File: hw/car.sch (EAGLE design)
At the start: 21 parts, among them Q1 BS170, Q2 BS170, Q3 BS170, Q4 BS170, Q5 BS170, Q6 BS170, Q7 BS170, Q8 BS170, X1 22-23-2041, X2 22-23-2041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

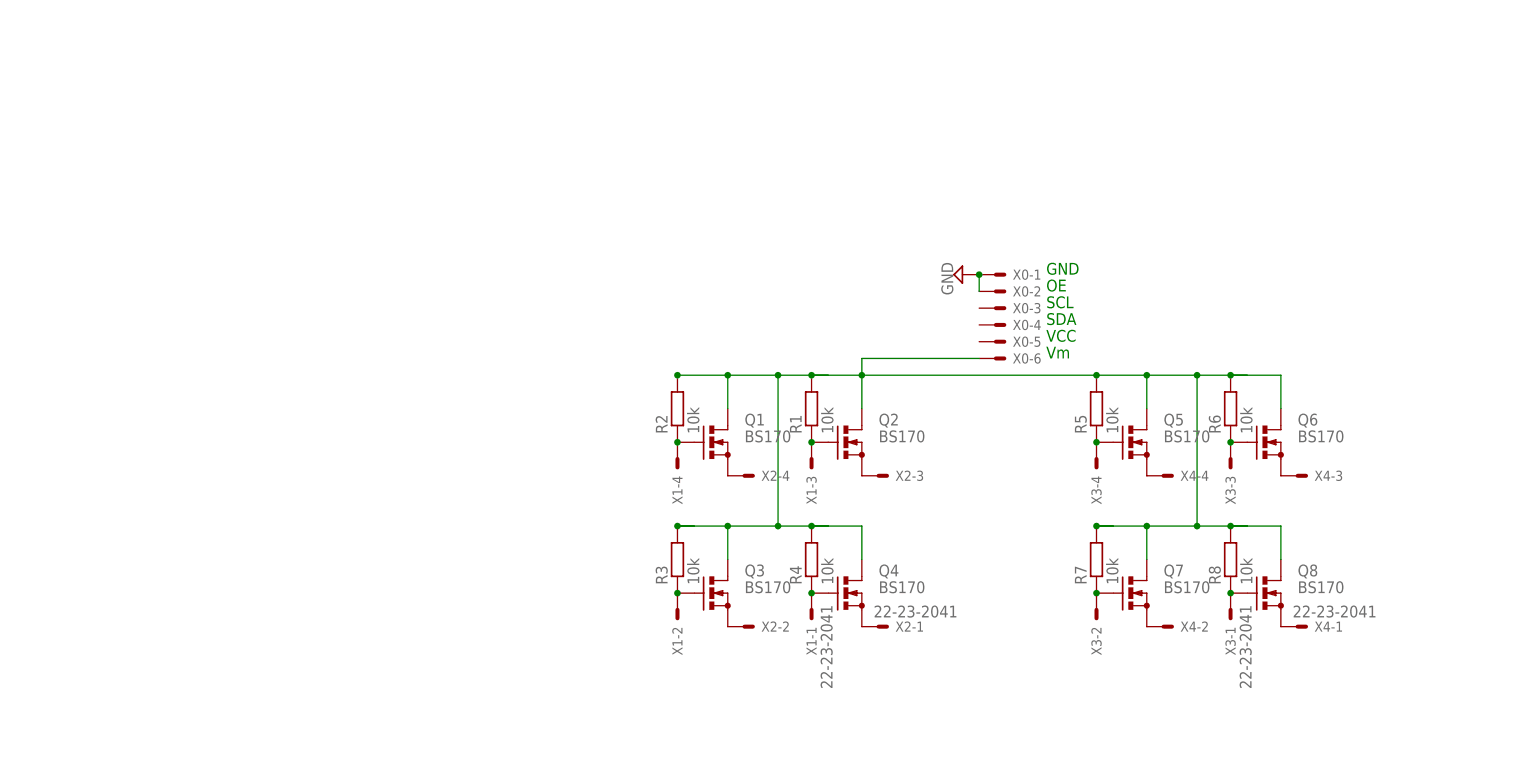
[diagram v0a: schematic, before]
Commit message: updated schematics
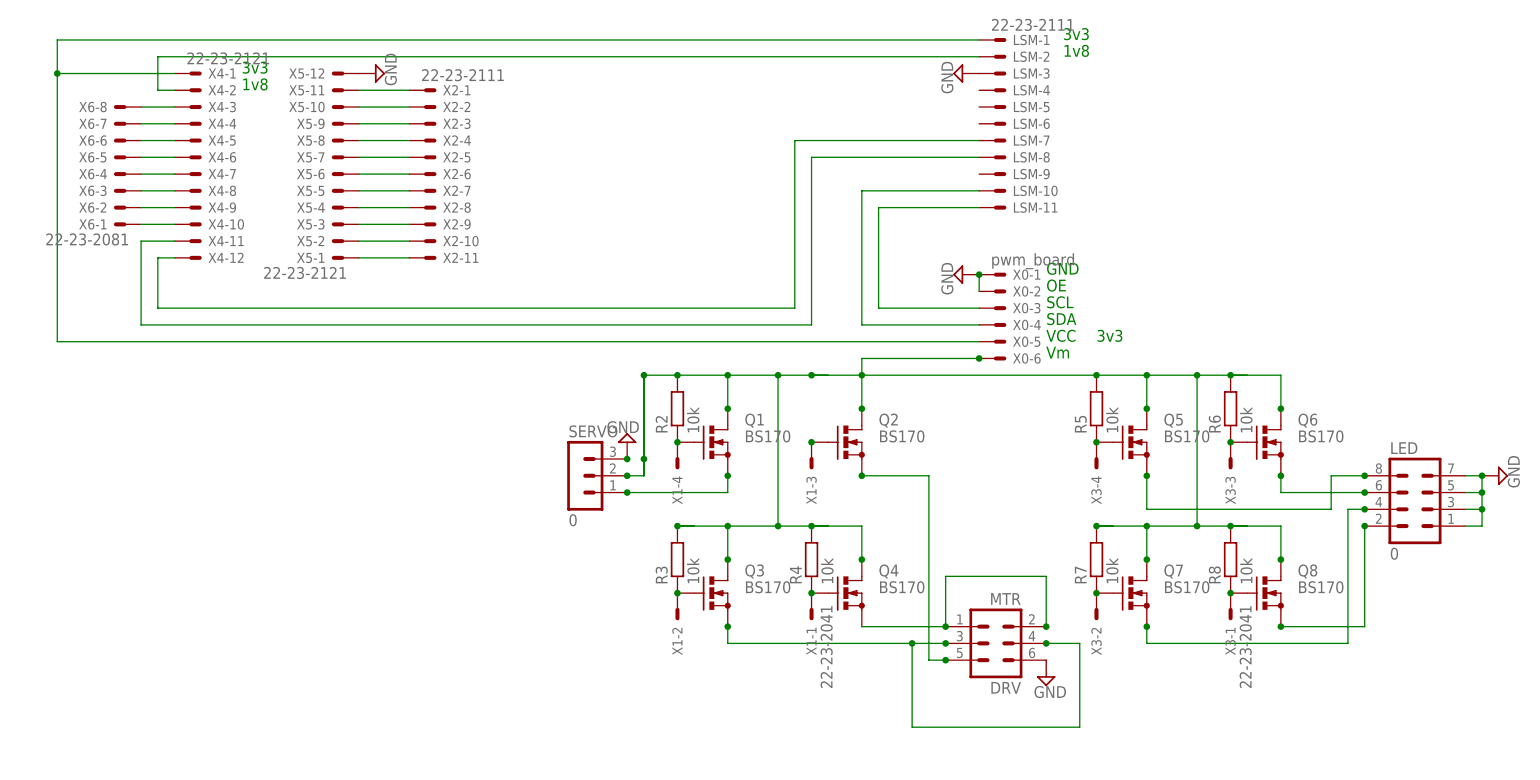
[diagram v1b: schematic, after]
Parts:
- removed R1: 10k, rcl:R-EU_0204/2V
- added DRV: MTR, con-lstb:MA03-2
- added LED: 0, con-lstb:MA04-2
- added LSM: 22-23-2111, con-molex:22-23-2111
- added SERVO: 0, con-lstb:MA03-1
- added X5: 22-23-2121, con-molex:22-23-2121
- added X6: 22-23-2081, con-molex:22-23-2081
- X0: value (none) -> pwm_board
- X2: value 22-23-2041 -> 22-23-2111; device con-molex:22-23-2041 -> con-molex:22-23-2111
- X4: value 22-23-2041 -> 22-23-2121; device con-molex:22-23-2041 -> con-molex:22-23-2121
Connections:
- new net N$18: LSM-10.S, X0-4.S
- new net N$19: LSM-11.S, X0-3.S
- new net N$20: LSM-8.S, X4-11.S
- new net N$21: LSM-7.S, X4-12.S
- new net N$22: X4-10.S, X6-1.S
- new net N$23: X4-9.S, X6-2.S
- new net N$24: X4-8.S, X6-3.S
- new net N$25: X4-7.S, X6-4.S
- new net N$26: X4-6.S, X6-5.S
- new net N$27: X4-5.S, X6-6.S
- new net N$28: X4-4.S, X6-7.S
- new net N$29: X4-3.S, X6-8.S
- new net N$30: X2-11.S, X5-1.S
- new net N$31: X2-10.S, X5-2.S
- new net N$32: X2-9.S, X5-3.S
- new net N$33: X2-8.S, X5-4.S
- new net N$34: X2-7.S, X5-5.S
- new net N$35: X2-6.S, X5-6.S
- new net N$36: X2-5.S, X5-7.S
- new net N$37: X2-4.S, X5-8.S
- new net N$38: X2-3.S, X5-9.S
- new net N$39: X2-2.S, X5-10.S
- new net N$40: X2-1.S, X5-11.S
- new net N$9: LED.2, Q8.S
- net GND: now also DRV.6, LED.1, LED.3, LED.5, LED.7, LSM-3.S, SERVO.3, X5-12.S
- net N$14: now also LED.4, Q7.S; no longer Q5.S, X4-4.S
- net N$15: now also LED.6; no longer X4-3.S
- net N$16: now also LED.8, Q5.S; no longer Q7.S, X4-2.S
- net N$17: now also LSM-2.S, X4-2.S; no longer Q8.S, X4-1.S
- net N$2: no longer R1.1
- net N$5: now also SERVO.1; no longer X2-4.S
- net N$6: now also DRV.1, DRV.2, Q4.S; no longer Q2.S, X2-3.S
- net N$7: now also DRV.3, DRV.4, DRV.5, Q2.S; no longer X2-2.S
- net N$8: now also LSM-1.S, X0-5.S, X4-1.S; no longer Q4.S, X2-1.S
- net VM: now also SERVO.2; no longer R1.2
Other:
- note added: "1v8"
- note added: "3v3"
- moved on the sheet: X2-1, X2-2, X2-3, X2-4, X4-1, X4-2, X4-3, X4-4

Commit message: layout started
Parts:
- added R1: 10k, rcl:R-EU_0204/2V
- renumbered X2 to OPT_R, X4 to SPRK_L, X5 to SPRK_R, X6 to OPT_L
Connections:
- new net N$41: DRV.6, Q2.S
- net GND: now also DRV.5; no longer DRV.6
- net N$2: now also R1.1
- net N$7: no longer DRV.5, Q2.S
- net VM: now also R1.2

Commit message: layout v1 done
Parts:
- removed DRV: MTR, con-lstb:MA03-2
- removed LED: 0, con-lstb:MA04-2
- removed OPT_L: 22-23-2081, con-molex:22-23-2081
- removed OPT_R: 22-23-2111, con-molex:22-23-2111
- removed Q2: BS170, transistor-small-signal:BS170
- removed R1, R8: 10k, rcl:R-EU_0204/2V
- added FL, FR, RL, RR: (no value), pinhead:PINHD-1X1
- added R0: 10k, rcl:R-EU_0207/10
- added R10, R9: 0, rcl:R-EU_0207/10
- added X2, X4: 22-23-2021, con-molex:22-23-2021
- R2, R3, R4, R5, R6, R7: device rcl:R-EU_0204/2V -> rcl:R-EU_0207/10
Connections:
- removed net N$15: LED.6, Q6.S
- removed net N$16: LED.8, Q5.S
- removed net N$23: OPT_L-2.S, SPRK_L-9.S
- removed net N$24: OPT_L-3.S, SPRK_L-8.S
- removed net N$25: OPT_L-4.S, SPRK_L-7.S
- removed net N$26: OPT_L-5.S, SPRK_L-6.S
- removed net N$27: OPT_L-6.S, SPRK_L-5.S
- removed net N$28: OPT_L-7.S, SPRK_L-4.S
- removed net N$29: OPT_L-8.S, SPRK_L-3.S
- removed net N$30: OPT_R-11.S, SPRK_R-1.S
- removed net N$31: OPT_R-10.S, SPRK_R-2.S
- removed net N$32: OPT_R-9.S, SPRK_R-3.S
- removed net N$33: OPT_R-8.S, SPRK_R-4.S
- removed net N$34: OPT_R-7.S, SPRK_R-5.S
- removed net N$35: OPT_R-6.S, SPRK_R-6.S
- removed net N$36: OPT_R-5.S, SPRK_R-7.S
- removed net N$37: OPT_R-4.S, SPRK_R-8.S
- removed net N$40: OPT_R-1.S, SPRK_R-11.S
- removed net N$41: DRV.6, Q2.S
- new net 1V8: LSM-2.S, R9.1
- new net V3V3: LSM-1.S, R10.2, X0-5.S
- net GND: no longer DRV.5, LED.1, LED.3, LED.5, LED.7
- net N$1: now also R0.1; no longer R2.1
- net N$10: now also R4.1; no longer R5.1
- net N$11: now also R5.1; no longer R6.1
- net N$12: now also R6.1; no longer R7.1
- net N$13: now also R7.1; no longer R8.1
- net N$14: now also FL.1; no longer LED.4
- net N$17: now also R9.2; no longer LSM-2.S
- net N$2: now also Q4.S, X2-1.S, X2-2.S; no longer Q2.G, R1.1, X1-3.S
- net N$22: now also R10.1, SPRK_L-1.S; no longer OPT_L-1.S, SPRK_L-10.S
- net N$3: now also R2.1; no longer R3.1
- net N$38: now also LSM-6.S; no longer OPT_R-3.S
- net N$39: now also LSM-5.S; no longer OPT_R-2.S
- net N$4: now also R3.1; no longer R4.1
- net N$6: now also Q5.S, RL.1; no longer DRV.1, DRV.2, Q4.S
- net N$7: now also Q6.S, RR.1; no longer DRV.3, DRV.4, Q3.S
- net N$8: now also Q3.S, X4-1.S, X4-2.S; no longer LSM-1.S, SPRK_L-1.S, X0-5.S
- net N$9: now also FR.1; no longer LED.2
- net VM: now also R0.2; no longer Q2.D, R1.2, R8.2
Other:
- moved on the sheet: R2, R3, R4, R5, R6, R7

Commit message: layout again
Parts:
- added FL-, RF-, RL-, RR-: (no value), pinhead:PINHD-1X1
- added R1, R8: 0, rcl:R-EU_0207/10
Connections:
- removed net N$38: LSM-6.S, SPRK_R-9.S
- removed net N$39: LSM-5.S, SPRK_R-10.S
- new net FILL: LSM-10.S, R8.1
- new net N$15: LSM-11.S, R1.1
- new net N$23: LSM-5.S, SPRK_R-9.S
- new net N$24: LSM-6.S, SPRK_R-10.S
- net GND: now also FL-.1, RF-.1, RL-.1, RR-.1
- net N$18: now also R8.2; no longer LSM-10.S
- net N$19: now also R1.2; no longer LSM-11.S
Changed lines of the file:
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@@
 <part name="RL" library="pinhead" deviceset="PINHD-1X1" device=""/>
 <part name="RR" library="pinhead" deviceset="PINHD-1X1" device=""/>
+<part name="RL-" library="pinhead" deviceset="PINHD-1X1" device=""/>
+<part name="RR-" library="pinhead" deviceset="PINHD-1X1" device=""/>
+<part name="RF-" library="pinhead" deviceset="PINHD-1X1" device=""/>
+<part name="FL-" library="pinhead" deviceset="PINHD-1X1" device=""/>
+<part name="SUPPLY2" library="supply2" deviceset="GND" device=""/>
+<part name="SUPPLY4" library="supply2" deviceset="GND" device=""/>
+<part name="SUPPLY7" library="supply2" deviceset="GND" device=""/>
+<part name="SUPPLY8" library="supply2" deviceset="GND" device=""/>
+<part name="R1" library="rcl" deviceset="R-EU_" device="0207/10" value="0"/>
+<part name="R8" library="rcl" deviceset="R-EU_" device="0207/10" value="0"/>
 </parts>
 <sheets>
@@
 <instance part="RL" gate="G$1" x="45.72" y="71.12" rot="R180"/>
 <instance part="RR" gate="G$1" x="106.68" y="71.12"/>
+<instance part="RL-" gate="G$1" x="45.72" y="78.74" rot="R180"/>
+<instance part="RR-" gate="G$1" x="106.68" y="78.74"/>
+<instance part="RF-" gate="G$1" x="99.06" y="33.02"/>
+<instance part="FL-" gate="G$1" x="68.58" y="33.02" rot="R180"/>
+<instance part="SUPPLY2" gate="GND" x="50.8" y="78.74" rot="R90"/>
+<instance part="SUPPLY4" gate="GND" x="73.66" y="33.02" rot="R90"/>
+<instance part="SUPPLY7" gate="GND" x="93.98" y="33.02" rot="R270"/>
+<instance part="SUPPLY8" gate="GND" x="101.6" y="78.74" rot="R270"/>
+<instance part="R1" gate="G$1" x="38.1" y="111.76" rot="R180"/>
+<instance part="R8" gate="G$1" x="35.56" y="114.3" rot="R180"/>
 </instances>
 <busses>
@@
 <pinref part="LSM" gate="-3" pin="S"/>
 <pinref part="SUPPLY6" gate="GND" pin="GND"/>
+</segment>
+<segment>
+<pinref part="RL-" gate="G$1" pin="1"/>
+<pinref part="SUPPLY2" gate="GND" pin="GND"/>
+</segment>
+<segment>
+<pinref part="FL-" gate="G$1" pin="1"/>
+<pinref part="SUPPLY4" gate="GND" pin="GND"/>
+</segment>
+<segment>
+<pinref part="RF-" gate="G$1" pin="1"/>
+<pinref part="SUPPLY7" gate="GND" pin="GND"/>
+</segment>
+<segment>
+<pinref part="RR-" gate="G$1" pin="1"/>
+<pinref part="SUPPLY8" gate="GND" pin="GND"/>
 </segment>
 </net>
@@
 <wire x1="45.72" y1="93.98" x2="27.94" y2="93.98" width="0.1524" layer="91"/>
 <wire x1="27.94" y1="93.98" x2="27.94" y2="114.3" width="0.1524" layer="91"/>
-<pinref part="LSM" gate="-10" pin="S"/>
-<wire x1="27.94" y1="114.3" x2="45.72" y2="114.3" width="0.1524" layer="91"/>
+<wire x1="27.94" y1="114.3" x2="30.48" y2="114.3" width="0.1524" layer="91"/>
+<pinref part="R8" gate="G$1" pin="2"/>
 </segment>
 </net>
@@
 <wire x1="45.72" y1="96.52" x2="30.48" y2="96.52" width="0.1524" layer="91"/>
 <wire x1="30.48" y1="96.52" x2="30.48" y2="111.76" width="0.1524" layer="91"/>
-<pinref part="LSM" gate="-11" pin="S"/>
-<wire x1="30.48" y1="111.76" x2="45.72" y2="111.76" width="0.1524" layer="91"/>
+<wire x1="30.48" y1="111.76" x2="33.02" y2="111.76" width="0.1524" layer="91"/>
+<pinref part="R1" gate="G$1" pin="2"/>
 </segment>
 </net>
@@
 </segment>
 </net>
-<net name="N$38" class="0">
-<segment>
-<pinref part="SPRK_R" gate="-9" pin="S"/>
-<pinref part="LSM" gate="-6" pin="S"/>
-<wire x1="-48.26" y1="124.46" x2="45.72" y2="124.46" width="0.1524" layer="91"/>
-</segment>
-</net>
-<net name="N$39" class="0">
-<segment>
-<pinref part="SPRK_R" gate="-10" pin="S"/>
-<pinref part="LSM" gate="-5" pin="S"/>
-<wire x1="-48.26" y1="127" x2="45.72" y2="127" width="0.1524" layer="91"/>
-</segment>
-</net>
 <net name="N$8" class="0">
 <segment>
@@
 </segment>
 </net>
+<net name="N$15" class="0">
+<segment>
+<pinref part="LSM" gate="-11" pin="S"/>
+<pinref part="R1" gate="G$1" pin="1"/>
+<wire x1="43.18" y1="111.76" x2="45.72" y2="111.76" width="0.1524" layer="91"/>
+</segment>
+</net>
+<net name="FILL" class="0">
+<segment>
+<pinref part="LSM" gate="-10" pin="S"/>
+<pinref part="R8" gate="G$1" pin="1"/>
+<wire x1="40.64" y1="114.3" x2="45.72" y2="114.3" width="0.1524" layer="91"/>
+</segment>
+</net>
+<net name="N$23" class="0">
+<segment>
+<pinref part="LSM" gate="-5" pin="S"/>
+<wire x1="45.72" y1="127" x2="-43.18" y2="127" width="0.1524" layer="91"/>
+<wire x1="-43.18" y1="127" x2="-43.18" y2="124.46" width="0.1524" layer="91"/>
+<pinref part="SPRK_R" gate="-9" pin="S"/>
+<wire x1="-43.18" y1="124.46" x2="-48.26" y2="124.46" width="0.1524" layer="91"/>
+</segment>
+</net>
+<net name="N$24" class="0">
+<segment>
+<pinref part="LSM" gate="-6" pin="S"/>
+<wire x1="45.72" y1="124.46" x2="-12.7" y2="124.46" width="0.1524" layer="91"/>
+<wire x1="-12.7" y1="124.46" x2="-12.7" y2="129.54" width="0.1524" layer="91"/>
+<wire x1="-12.7" y1="129.54" x2="-45.72" y2="129.54" width="0.1524" layer="91"/>
+<wire x1="-45.72" y1="129.54" x2="-45.72" y2="127" width="0.1524" layer="91"/>
+<pinref part="SPRK_R" gate="-10" pin="S"/>
+<wire x1="-45.72" y1="127" x2="-48.26" y2="127" width="0.1524" layer="91"/>
+</segment>
+</net>
